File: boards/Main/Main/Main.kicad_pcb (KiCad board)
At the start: 2 copper layers, 80 x 100 mm, 33 parts, among them Q1 2N3904, Q2 2N3904, Q3 2N3904

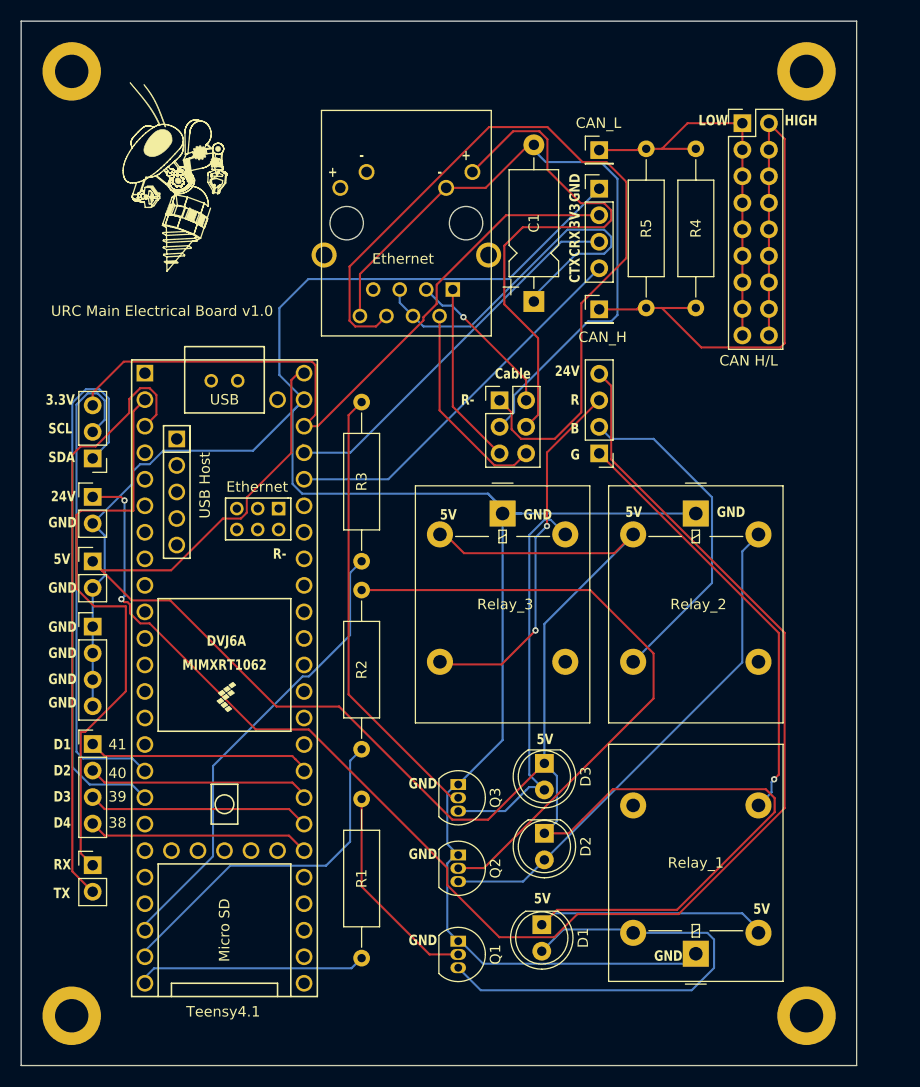
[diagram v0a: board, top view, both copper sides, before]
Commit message: Prepared Boards for PCB Manufacture
Added GND line for IMU on Main Board
Fixed Silkscreen Text Size for PCB Manufacture on Science, Main, and Arm boards
Generated Gerber Files for Science, Main, and Arm boards
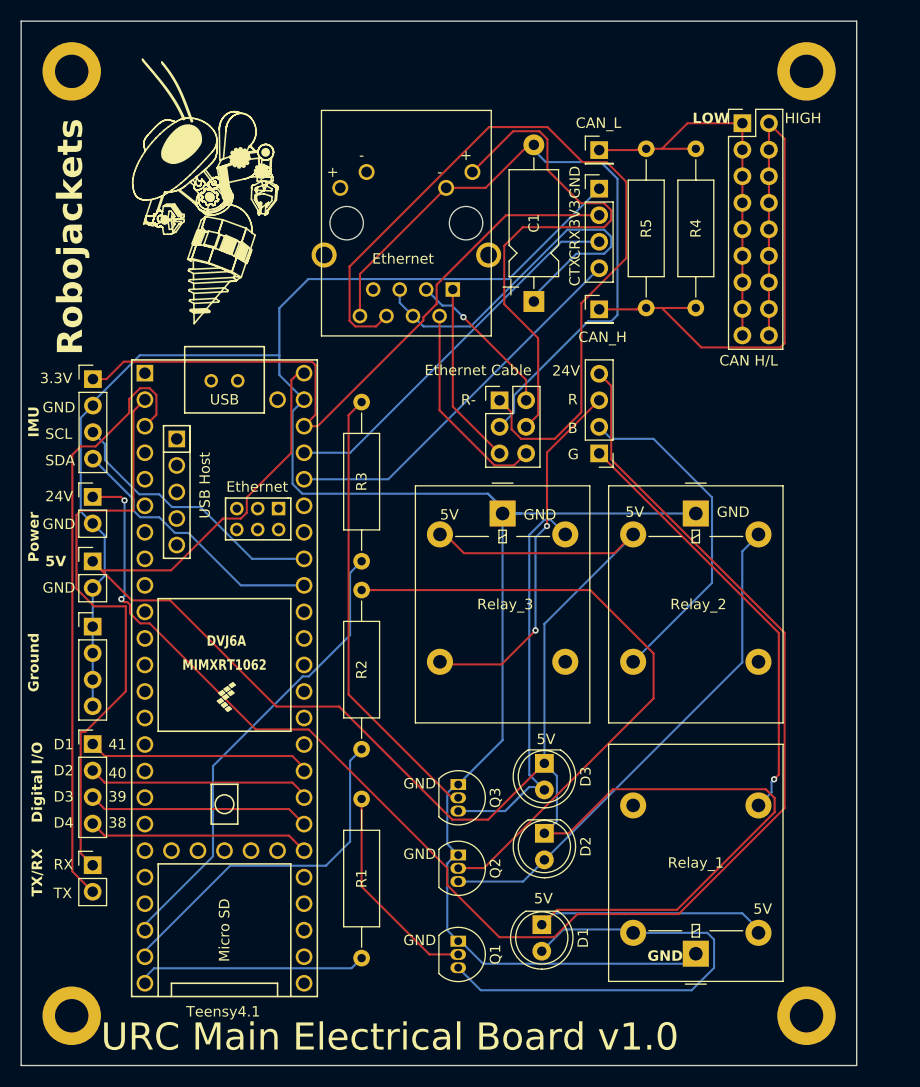
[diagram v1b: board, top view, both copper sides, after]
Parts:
- IMU1: value IMU -> GND; footprint Connector_PinHeader_2.54mm:PinHeader_1x03_P2.54mm_Vertical -> Connector_PinHeader_2.54mm:PinHeader_1x04_P2.54mm_Vertical
- moved IMU1 7.60 mm to (96.8, 74.9), turned to 0 degrees
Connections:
- IMU1 pad 1: /SDA2 -> /3.3V
- IMU1 pad 2: /SCL2 -> GND
- IMU1 pad 3: /3.3V -> /SCL
- Teensy4.1 pad 16: /SCL2 -> unconnected-(Teensy4.1-24_A10_TX6_SCL2-Pad16)
- Teensy4.1 pad 17: /SDA2 -> unconnected-(Teensy4.1-25_A11_RX6_SDA2-Pad17)
- Teensy4.1 pad 40: unconnected-(Teensy4.1-18_A4_SDA-Pad40) -> /SDA
- Teensy4.1 pad 41: unconnected-(Teensy4.1-19_A5_SCL-Pad41) -> /SCL
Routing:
- net /SDA2: track 53.8 -> 0.00 mm
- net /SCL2: track 47.5 -> 0.00 mm
- net /SCL: track 0.00 -> 26.1 mm
- net /SDA: track 0.00 -> 25.9 mm
- net GND: track 212.5 -> 219.0 mm
- net /3.3V: track 68.1 -> 66.3 mm
- net Net-(Q3-B): track 43.6 -> 43.1 mm
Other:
- board text added: "Ethernet Cable"
- board text added: "Ground"
- board text added: "IMU"
- board text added: "Power"
- board text added: "Robojackets"
- board text removed: "Cable"
